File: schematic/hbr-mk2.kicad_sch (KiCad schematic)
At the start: 34 parts, among them J1 Barrel_Jack, J3 AudioJack3, Q1 IRF4905, Q2 2N7000, Q3 2N7000, Q4 IRF4905, SW1 SW_SPST, SW10 SW_Push, SW11 RotaryEncoder_Switch, SW2 SW_SPST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

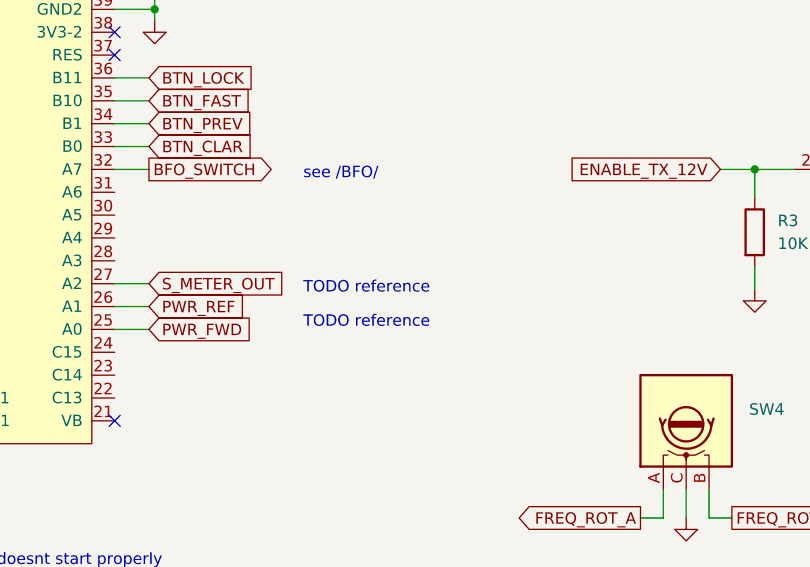
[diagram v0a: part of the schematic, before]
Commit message: Schematic: add S-meter
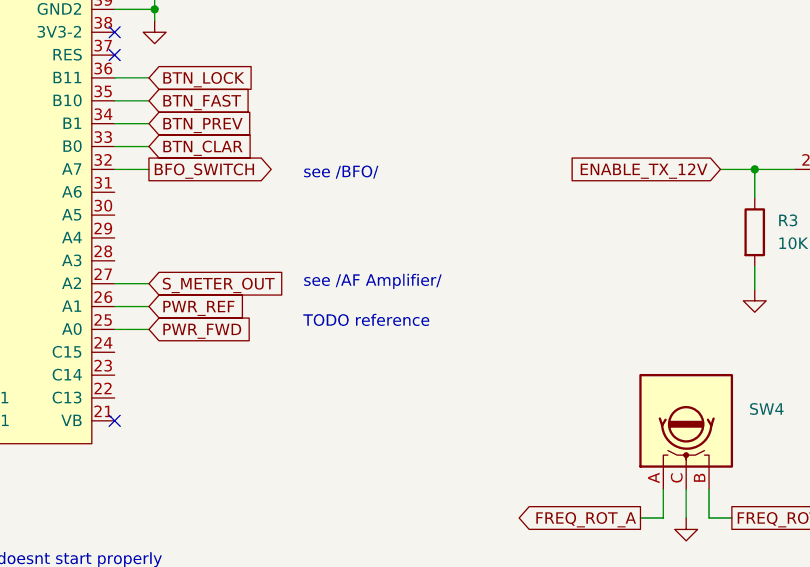
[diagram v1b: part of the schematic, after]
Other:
- note added: "see /AF Amplifier/"
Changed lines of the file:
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@@
     (effects (font (size 1.27 1.27)) (justify left bottom))
   )
-  (text "TODO reference" (at 177.8 98.425 0)
+  (text "see /AF Amplifier/" (at 177.8 97.79 0)
     (effects (font (size 1.27 1.27)) (justify left bottom))
   )

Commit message: Add CW tone generator + other changes
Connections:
- net ENABLE_CW_TONE: now reaches U1.22 (C13)
- net ENABLE_CW_TX: now reaches U1.23 (C14)
- net LPF_SEL_12_10: now reaches U1.24 (C15)
- net LPF_SEL_15_17: now reaches U1.28 (A3)
- net LPF_SEL_20_30: now reaches U1.29 (A4)
- net LPF_SEL_40: now reaches U1.30 (A5)
- net LPF_SEL_80: now reaches U1.31 (A6)
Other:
- added sheet CW Tone (cw-tone.kicad_sch)
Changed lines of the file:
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@@
+    (stroke (width 0) (type default))
+  )
+  (wire (pts (xy 156.845 104.775) (xy 160.655 104.775))
     (stroke (width 0) (type default))
   )
@@
     (stroke (width 0) (type default))
   )
+  (wire (pts (xy 156.845 109.855) (xy 160.655 109.855))
+    (stroke (width 0) (type default))
+  )
   (wire (pts (xy 145.415 31.75) (xy 149.86 31.75))
     (stroke (width 0) (type default))
@@
     (stroke (width 0) (type default))
   )
+  (wire (pts (xy 156.845 86.995) (xy 160.655 86.995))
+    (stroke (width 0) (type default))
+  )
+  (wire (pts (xy 156.845 107.315) (xy 160.655 107.315))
+    (stroke (width 0) (type default))
+  )
   (wire (pts (xy 161.29 66.675) (xy 161.29 64.135))
     (stroke (width 0) (type default))
@@
     (stroke (width 0) (type default))
   )
+  (wire (pts (xy 156.845 89.535) (xy 160.655 89.535))
+    (stroke (width 0) (type default))
+  )
   (wire (pts (xy 133.35 99.695) (xy 136.525 99.695))
     (stroke (width 0) (type default))
@@
     (stroke (width 0) (type default))
   )
+  (wire (pts (xy 156.845 94.615) (xy 160.655 94.615))
+    (stroke (width 0) (type default))
+  )
   (wire (pts (xy 268.605 150.495) (xy 271.78 150.495))
     (stroke (width 0) (type default))
@@
   )
   (wire (pts (xy 128.27 43.18) (xy 128.27 45.085))
+    (stroke (width 0) (type default))
+  )
+  (wire (pts (xy 156.845 92.075) (xy 160.655 92.075))
     (stroke (width 0) (type default))
   )
@@
     )
   )
+  (global_label "LPF_SEL_80" (shape output) (at 160.655 86.995 0) (fields_autoplaced)
+    (effects (font (size 1.27 1.27)) (justify left))
+    (property "Intersheetrefs" "${INTERSHEET_REFS}" (at 174.6883 86.995 0)
+      (effects (font (size 1.27 1.27)) (justify left) hide)
+    )
+  )
   (global_label "PWR_FWD" (shape input) (at 160.655 102.235 0) (fields_autoplaced)
     (effects (font (size 1.27 1.27)) (justify left))
@@
     )
   )
+  (global_label "LPF_SEL_20_30" (shape output) (at 160.655 92.075 0) (fields_autoplaced)
+    (effects (font (size 1.27 1.27)) (justify left))
+    (property "Intersheetrefs" "${INTERSHEET_REFS}" (at 178.0749 92.075 0)
+      (effects (font (size 1.27 1.27)) (justify left) hide)
+    )
+  )
   (global_label "FREQ_ROT_A" (shape input) (at 133.35 74.295 180) (fields_autoplaced)
     (effects (font (size 1.27 1.27)) (justify right))
@@
     (property "Intersheetrefs" "${INTERSHEET_REFS}" (at 242.3252 141.605 0)
       (effects (font (size 1.27 1.27)) (justify right) hide)
+    )
+  )
+  (global_label "LPF_SEL_12_10" (shape output) (at 160.655 104.775 0) (fields_autoplaced)
+    (effects (font (size 1.27 1.27)) (justify left))
+    (property "Intersheetrefs" "${INTERSHEET_REFS}" (at 178.0749 104.775 0)
+      (effects (font (size 1.27 1.27)) (justify left) hide)
     )
   )
@@
     )
   )
+  (global_label "ENABLE_CW_TX" (shape output) (at 160.655 107.315 0) (fields_autoplaced)
+    (effects (font (size 1.27 1.27)) (justify left))
+    (property "Intersheetrefs" "${INTERSHEET_REFS}" (at 177.4097 107.315 0)
+      (effects (font (size 1.27 1.27)) (justify left) hide)
+    )
+  )
   (global_label "KEY_DAH" (shape output) (at 132.715 154.305 0) (fields_autoplaced)
     (effects (font (size 1.27 1.27)) (justify left))
@@
     )
   )
+  (global_label "LPF_SEL_40" (shape output) (at 160.655 89.535 0) (fields_autoplaced)
+    (effects (font (size 1.27 1.27)) (justify left))
+    (property "Intersheetrefs" "${INTERSHEET_REFS}" (at 174.6883 89.535 0)
+      (effects (font (size 1.27 1.27)) (justify left) hide)
+    )
+  )
   (global_label "CLAR_ROT_B" (shape input) (at 133.35 89.535 180) (fields_autoplaced)
     (effects (font (size 1.27 1.27)) (justify right))
@@
     )
   )
+  (global_label "LPF_SEL_15_17" (shape output) (at 160.655 94.615 0) (fields_autoplaced)
+    (effects (font (size 1.27 1.27)) (justify left))
+    (property "Intersheetrefs" "${INTERSHEET_REFS}" (at 178.0749 94.615 0)
+      (effects (font (size 1.27 1.27)) (justify left) hide)
+    )
+  )
   (global_label "RF_AMP_BYPASS_12V" (shape output) (at 145.415 186.69 0) (fields_autoplaced)
     (effects (font (size 1.27 1.27)) (justify left))
@@
     (property "Intersheetrefs" "${INTERSHEET_REFS}" (at 203.1668 139.7 0)
       (effects (font (size 1.27 1.27)) (justify right) hide)
+    )
+  )
+  (global_label "ENABLE_CW_TONE" (shape output) (at 160.655 109.855 0) (fields_autoplaced)
+    (effects (font (size 1.27 1.27)) (justify left))
+    (property "Intersheetrefs" "${INTERSHEET_REFS}" (at 180.0102 109.855 0)
+      (effects (font (size 1.27 1.27)) (justify left) hide)
     )
   )
@@
       )
     )
+  )
+  (sheet (at 19.05 132.08) (size 18.415 8.255) (fields_autoplaced)
+    (stroke (width 0.1524) (type solid))
+    (fill (color 0 0 0 0.0000))
+    (property "Sheetname" "CW Tone" (at 19.05 131.3684 0)
+      (effects (font (size 1.27 1.27)) (justify left bottom))
+    )
+    (property "Sheetfile" "cw-tone.kicad_sch" (at 19.05 140.9196 0)
+      (effects (font (size 1.27 1.27)) (justify left top))
+    )
+    (instances
+      (project "hbr-mk2"
+        (path "/700c9878-4ed7-49d5-a273-77cf9d92989d" (page "10"))
+      )
+    )

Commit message: Rename ENABLE_CW_TX to ENABLE_TX
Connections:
- net ENABLE_CW_TX renamed ENABLE_TX
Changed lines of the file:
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@@
     )
   )
-  (global_label "ENABLE_CW_TX" (shape output) (at 160.655 107.315 0) (fields_autoplaced)
+  (global_label "ENABLE_TX" (shape output) (at 160.655 107.315 0) (fields_autoplaced)
     (effects (font (size 1.27 1.27)) (justify left))
-    (property "Intersheetrefs" "${INTERSHEET_REFS}" (at 177.4097 107.315 0)
+    (property "Intersheetrefs" "${INTERSHEET_REFS}" (at 173.7207 107.315 0)
       (effects (font (size 1.27 1.27)) (justify left) hide)
     )

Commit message: Rename ENABLE_TX to ENABLE_KEYED_VCC
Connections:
- net ENABLE_TX renamed ENABLE_KEYED_VCC
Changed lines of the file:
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@@
     )
   )
-  (global_label "ENABLE_TX" (shape output) (at 160.655 107.315 0) (fields_autoplaced)
+  (global_label "ENABLE_KEYED_VCC" (shape output) (at 160.655 107.315 0) (fields_autoplaced)
     (effects (font (size 1.27 1.27)) (justify left))
-    (property "Intersheetrefs" "${INTERSHEET_REFS}" (at 173.7207 107.315 0)
+    (property "Intersheetrefs" "${INTERSHEET_REFS}" (at 182.0664 107.315 0)
       (effects (font (size 1.27 1.27)) (justify left) hide)
     )

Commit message: Add /TX Common/ schematic sheet
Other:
- added sheet TX Common (tx-common.kicad_sch)
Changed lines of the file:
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@@
+    )
+  )
+  (sheet (at 19.05 146.05) (size 18.415 8.255) (fields_autoplaced)
+    (stroke (width 0.1524) (type solid))
+    (fill (color 0 0 0 0.0000))
+    (property "Sheetname" "TX Common" (at 19.05 145.3384 0)
+      (effects (font (size 1.27 1.27)) (justify left bottom))
+    )
+    (property "Sheetfile" "tx-common.kicad_sch" (at 19.05 154.8896 0)
+      (effects (font (size 1.27 1.27)) (justify left top))
+    )
+    (instances
+      (project "hbr-mk2"
+        (path "/700c9878-4ed7-49d5-a273-77cf9d92989d" (page "11"))
+      )
     )
   )

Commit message: Schematic: minor changes
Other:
- note added: "see /CW Tone/"
- note added: "see /TX Common/"
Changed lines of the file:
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@@
     (stroke (width 0) (type default))
   )
-  (text "TODO reference" (at 177.8 102.235 0)
+  (text "TODO reference" (at 172.72 102.235 0)
     (effects (font (size 1.27 1.27)) (justify left bottom))
   )
@@
     (effects (font (size 1.27 1.27)) (justify left bottom))
   )
-  (text "see /AF Amplifier/" (at 177.8 97.79 0)
+  (text "see /AF Amplifier/" (at 176.53 98.425 0)
     (effects (font (size 1.27 1.27)) (justify left bottom))
   )
@@
     (effects (font (size 1.27 1.27)) (justify left bottom))
   )
+  (text "see /TX Common/" (at 182.88 108.585 0)
+    (effects (font (size 1.27 1.27)) (justify left bottom))
+  )
   (text "B8 & B9 are 5V-tolerant" (at 116.84 119.38 0)
     (effects (font (size 1.27 1.27)) (justify left bottom))
   )
-  (text "see /BFO/" (at 177.8 85.725 0)
+  (text "see /BFO/" (at 176.53 85.725 0)
     (effects (font (size 1.27 1.27)) (justify left bottom))
   )
@@
     (effects (font (size 1.27 1.27)) (justify left bottom))
   )
+  (text "see /CW Tone/" (at 182.88 111.125 0)
+    (effects (font (size 1.27 1.27)) (justify left bottom))
+  )

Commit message: Add PA schematic + some minor changes
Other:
- added sheet Power Amplifier (power-amplifier.kicad_sch)
- note added: "== General notes == - HFD4/12 relay is a full equivalent of G6K-2F-Y - KT3142A transistor is a full equvalent of 2N2369A - KT3142A can be replaced with another transistor with fT >= 500 Mhz - ADE-6 mixers can be replaced with ADE-1, ADE-2, etc"
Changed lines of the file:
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@@
+    (effects (font (size 1.27 1.27)) (justify left bottom))
+  )
+  (text "== General notes ==\n- HFD4/12 relay is a full equivalent of G6K-2F-Y\n- KT3142A transistor is a full equvalent of 2N2369A\n- KT3142A can be replaced with another transistor with fT >= 500 Mhz\n- ADE-6 mixers can be replaced with ADE-1, ADE-2, etc"
+    (at 176.53 27.94 0)
     (effects (font (size 1.27 1.27)) (justify left bottom))
   )
@@
       )
     )
+  )
+  (sheet (at 19.05 160.02) (size 18.415 8.255) (fields_autoplaced)
+    (stroke (width 0.1524) (type solid))
+    (fill (color 0 0 0 0.0000))
+    (property "Sheetname" "Power Amplifier" (at 19.05 159.3084 0)
+      (effects (font (size 1.27 1.27)) (justify left bottom))
+    )
+    (property "Sheetfile" "power-amplifier.kicad_sch" (at 19.05 168.8596 0)
+      (effects (font (size 1.27 1.27)) (justify left top))
+    )
+    (instances
+      (project "hbr-mk2"
+        (path "/700c9878-4ed7-49d5-a273-77cf9d92989d" (page "12"))
+      )
+    )

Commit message: Schematic: add low pass filters
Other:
- added sheet LPFs (lpfs.kicad_sch)
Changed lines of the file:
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@@
+    )
+  )
+  (sheet (at 19.05 173.99) (size 18.415 8.255) (fields_autoplaced)
+    (stroke (width 0.1524) (type solid))
+    (fill (color 0 0 0 0.0000))
+    (property "Sheetname" "LPFs" (at 19.05 173.2784 0)
+      (effects (font (size 1.27 1.27)) (justify left bottom))
+    )
+    (property "Sheetfile" "lpfs.kicad_sch" (at 19.05 182.8296 0)
+      (effects (font (size 1.27 1.27)) (justify left top))
+    )
+    (instances
+      (project "hbr-mk2"
+        (path "/700c9878-4ed7-49d5-a273-77cf9d92989d" (page "13"))
+      )
     )
   )
